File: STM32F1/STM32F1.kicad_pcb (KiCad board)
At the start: 2 copper layers, 55.9 x 22.9 mm, 40 parts, among them J1 Conn_02x03_Odd_Even, J2 Conn_01x04_Male, J3 10033526-N3212MLF, J4 Conn_01x20_Male, J5 Conn_01x20_Male, SW1 PTS 647 SK38 SMTR2 LFS, U1 RT9193, U2 STM32F103CBTx, Y1 ABL-8.000MHZ-B2‎, Y2 RSM200S-32.768-12.5-10PPM-NPB

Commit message: Boards sent to be built.
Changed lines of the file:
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@@
     (thickness 1.6)
     (drawings 58)
-    (tracks 398)
+    (tracks 393)
     (zones 0)
     (modules 40)
@@
   (segment (start 166.878 101.219) (end 166.878 101.219) (width 0.2032) (layer F.Cu) (net 3))
   (via (at 164.211 101.6) (size 0.6096) (drill 0.3048) (layers F.Cu B.Cu) (net 3))
-  (segment (start 160.909 101.727) (end 159.512 101.727) (width 0.2032) (layer B.Cu) (net 3))
-  (segment (start 164.211 101.6) (end 161.163 101.6) (width 0.2032) (layer B.Cu) (net 3))
-  (segment (start 161.036 101.727) (end 160.909 101.727) (width 0.2032) (layer B.Cu) (net 3))
-  (segment (start 161.163 101.6) (end 161.036 101.727) (width 0.2032) (layer B.Cu) (net 3))
   (segment (start 168.783 101.219) (end 164.592 101.219) (width 0.2032) (layer F.Cu) (net 3))
   (segment (start 169.771555 99.749891) (end 169.744109 99.749891) (width 0.2032) (layer F.Cu) (net 3))
@@
   (segment (start 169.744109 99.749891) (end 169.164 100.33) (width 0.2032) (layer F.Cu) (net 3))
   (segment (start 169.164 100.838) (end 168.783 101.219) (width 0.2032) (layer F.Cu) (net 3))
+  (segment (start 164.211 101.6) (end 161.163 101.6) (width 0.2032) (layer B.Cu) (net 3))
+  (segment (start 161.036 101.727) (end 159.512 101.727) (width 0.2032) (layer B.Cu) (net 3))
+  (segment (start 161.163 101.6) (end 161.036 101.727) (width 0.2032) (layer B.Cu) (net 3))
   (via (at 165.608 102.362) (size 0.9144) (drill 0.4572) (layers F.Cu B.Cu) (net 4))
   (via (at 191.389 96.8375) (size 0.6096) (drill 0.3048) (layers F.Cu B.Cu) (net 4))
@@
   (segment (start 167.64 108.712) (end 186.944 108.712) (width 0.2032) (layer B.Cu) (net 8))
   (segment (start 186.944 108.712) (end 187.96 107.696) (width 0.2032) (layer B.Cu) (net 8))
+  (segment (start 189.879 103.491) (end 189.23 104.14) (width 0.2032) (layer B.Cu) (net 9))
+  (segment (start 191.389 103.491) (end 189.879 103.491) (width 0.2032) (layer B.Cu) (net 9))
+  (segment (start 190.627 105.537) (end 189.23 104.14) (width 0.2032) (layer F.Cu) (net 9))
+  (segment (start 165.227 111.76) (end 183.896 111.76) (width 0.2032) (layer F.Cu) (net 9))
+  (segment (start 165.299105 107.050769) (end 164.476074 107.8738) (width 0.2032) (layer F.Cu) (net 9))
+  (segment (start 164.465 110.998) (end 165.227 111.76) (width 0.2032) (layer F.Cu) (net 9))
+  (segment (start 183.896 111.76) (end 184.785 110.871) (width 0.2032) (layer F.Cu) (net 9))
+  (segment (start 164.476074 107.8738) (end 164.465 107.8738) (width 0.2032) (layer F.Cu) (net 9))
+  (segment (start 184.785 110.871) (end 184.785 109.982) (width 0.2032) (layer F.Cu) (net 9))
   (segment (start 190.627 108.077) (end 190.627 105.537) (width 0.2032) (layer F.Cu) (net 9))
   (segment (start 164.465 107.8738) (end 164.465 110.998) (width 0.2032) (layer F.Cu) (net 9))
+  (segment (start 184.785 109.982) (end 185.547 109.22) (width 0.2032) (layer F.Cu) (net 9))
+  (segment (start 185.547 109.22) (end 189.484 109.22) (width 0.2032) (layer F.Cu) (net 9))
   (segment (start 189.484 109.22) (end 190.627 108.077) (width 0.2032) (layer F.Cu) (net 9))
-  (segment (start 165.227 111.76) (end 183.769 111.633) (width 0.2032) (layer F.Cu) (net 9))
-  (segment (start 165.299105 107.050769) (end 164.476074 107.8738) (width 0.2032) (layer F.Cu) (net 9))
-  (segment (start 164.465 110.998) (end 165.227 111.76) (width 0.2032) (layer F.Cu) (net 9))
-  (segment (start 183.769 111.633) (end 184.023 111.633) (width 0.2032) (layer F.Cu) (net 9))
-  (segment (start 185.547 109.22) (end 189.484 109.22) (width 0.2032) (layer F.Cu) (net 9))
-  (segment (start 164.476074 107.8738) (end 164.465 107.8738) (width 0.2032) (layer F.Cu) (net 9))
-  (segment (start 190.627 105.537) (end 189.23 104.14) (width 0.2032) (layer F.Cu) (net 9))
-  (segment (start 184.785 109.982) (end 185.547 109.22) (width 0.2032) (layer F.Cu) (net 9))
-  (segment (start 184.023 111.633) (end 184.785 110.871) (width 0.2032) (layer F.Cu) (net 9))
-  (segment (start 184.785 110.871) (end 184.785 109.982) (width 0.2032) (layer F.Cu) (net 9))
-  (segment (start 189.879 103.491) (end 189.23 104.14) (width 0.2032) (layer B.Cu) (net 9))
-  (segment (start 191.389 103.491) (end 189.879 103.491) (width 0.2032) (layer B.Cu) (net 9))
   (via (at 145.529 102.87) (size 0.6096) (drill 0.3048) (layers F.Cu B.Cu) (net 10))
   (segment (start 145.529 103.391) (end 145.529 102.87) (width 0.2032) (layer B.Cu) (net 10))
@@
   (segment (start 160.655 110.49) (end 160.655 110.28066) (width 0.2032) (layer F.Cu) (net 34))
   (segment (start 147.447 111.633) (end 146.685 110.871) (width 0.2032) (layer B.Cu) (net 34))
+  (segment (start 145.7325 108.9025) (end 145.7325 107.555) (width 0.2032) (layer B.Cu) (net 34))
+  (segment (start 146.685 109.855) (end 145.7325 108.9025) (width 0.2032) (layer B.Cu) (net 34))
+  (segment (start 146.685 110.871) (end 146.685 109.855) (width 0.2032) (layer B.Cu) (net 34))
+  (segment (start 160.655 110.617) (end 159.639 111.633) (width 0.2032) (layer B.Cu) (net 34))
+  (segment (start 160.655 110.49) (end 160.655 110.617) (width 0.2032) (layer B.Cu) (net 34))
   (segment (start 159.639 111.633) (end 147.447 111.633) (width 0.2032) (layer B.Cu) (net 34))
-  (segment (start 160.655 110.49) (end 160.655 110.617) (width 0.2032) (layer B.Cu) (net 34))
-  (segment (start 160.655 110.617) (end 159.639 111.633) (width 0.2032) (layer B.Cu) (net 34))
-  (segment (start 146.685 110.871) (end 146.685 109.855) (width 0.2032) (layer B.Cu) (net 34))
-  (segment (start 146.685 109.855) (end 145.7325 108.9025) (width 0.2032) (layer B.Cu) (net 34))
-  (segment (start 145.7325 108.9025) (end 145.7325 107.555) (width 0.2032) (layer B.Cu) (net 34))
   (segment (start 163.195 108.447766) (end 164.945551 106.697215) (width 0.2032) (layer F.Cu) (net 35))
   (segment (start 163.195 110.49) (end 163.195 108.447766) (width 0.2032) (layer F.Cu) (net 35))
   (segment (start 145.0975 112.0775) (end 144.145 111.125) (width 0.2032) (layer B.Cu) (net 35))
+  (segment (start 161.6075 112.0775) (end 145.0975 112.0775) (width 0.2032) (layer B.Cu) (net 35))
+  (segment (start 144.145 111.125) (end 144.145 107.555) (width 0.2032) (layer B.Cu) (net 35))
   (segment (start 163.195 110.49) (end 161.6075 112.0775) (width 0.2032) (layer B.Cu) (net 35))
-  (segment (start 144.145 111.125) (end 144.145 107.555) (width 0.2032) (layer B.Cu) (net 35))
-  (segment (start 161.6075 112.0775) (end 145.0975 112.0775) (width 0.2032) (layer B.Cu) (net 35))
   (segment (start 142.635 107.555) (end 144.145 107.555) (width 0.2032) (layer B.Cu) (net 35))
   (segment (start 140.335 109.855) (end 142.635 107.555) (width 0.2032) (layer B.Cu) (net 35))
@@
   (segment (start 167.132 99.314) (end 167.513 99.695) (width 0.381) (layer F.Cu) (net 52))
   (segment (start 168.412234 99.695) (end 169.064449 99.042785) (width 0.381) (layer F.Cu) (net 52))
-  (segment (start 186.055 110.49) (end 184.277 112.268) (width 0.508) (layer F.Cu) (net 53))
-  (segment (start 149.225 111.76) (end 149.225 109.728) (width 0.508) (layer F.Cu) (net 53))
-  (segment (start 149.86 112.395) (end 149.225 111.76) (width 0.508) (layer F.Cu) (net 53))
-  (segment (start 150.114 112.395) (end 149.86 112.395) (width 0.508) (layer F.Cu) (net 53))
-  (segment (start 160.655 112.395) (end 150.114 112.395) (width 0.508) (layer F.Cu) (net 53))
-  (segment (start 184.15 112.395) (end 160.655 112.395) (width 0.508) (layer F.Cu) (net 53))
-  (segment (start 184.277 112.268) (end 184.15 112.395) (width 0.508) (layer F.Cu) (net 53))
   (segment (start 149.225 109.728) (end 149.225 109.728) (width 0.508) (layer F.Cu) (net 53))
   (via (at 149.225 109.728) (size 0.6096) (drill 0.3048) (layers F.Cu B.Cu) (net 53))
   (segment (start 149.225 109.454) (end 147.574 107.803) (width 0.508) (layer B.Cu) (net 53))
   (segment (start 149.225 109.728) (end 149.225 109.454) (width 0.508) (layer B.Cu) (net 53))
+  (segment (start 149.86 112.395) (end 149.225 111.76) (width 0.508) (layer F.Cu) (net 53))
+  (segment (start 149.225 111.76) (end 149.225 109.728) (width 0.508) (layer F.Cu) (net 53))
+  (segment (start 186.055 110.49) (end 184.15 112.395) (width 0.508) (layer F.Cu) (net 53))
+  (segment (start 184.15 112.395) (end 149.86 112.395) (width 0.508) (layer F.Cu) (net 53))
   (zone (net 1) (net_name GND) (layer B.Cu) (hatch edge 0.508)
     (connect_pads (clearance 0.1524))

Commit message: Update values on PCB.
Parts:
- R10: value 10k -> 2.4k
- R11: value 10k -> 1k

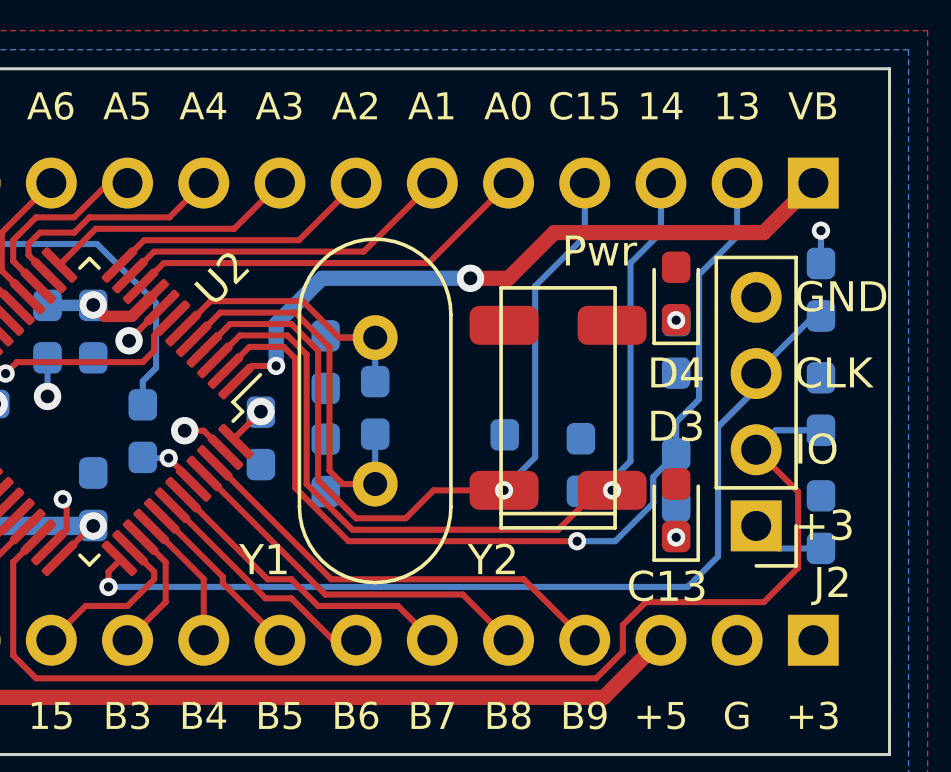
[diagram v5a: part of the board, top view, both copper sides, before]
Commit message: STM32F1 board with different crystals.
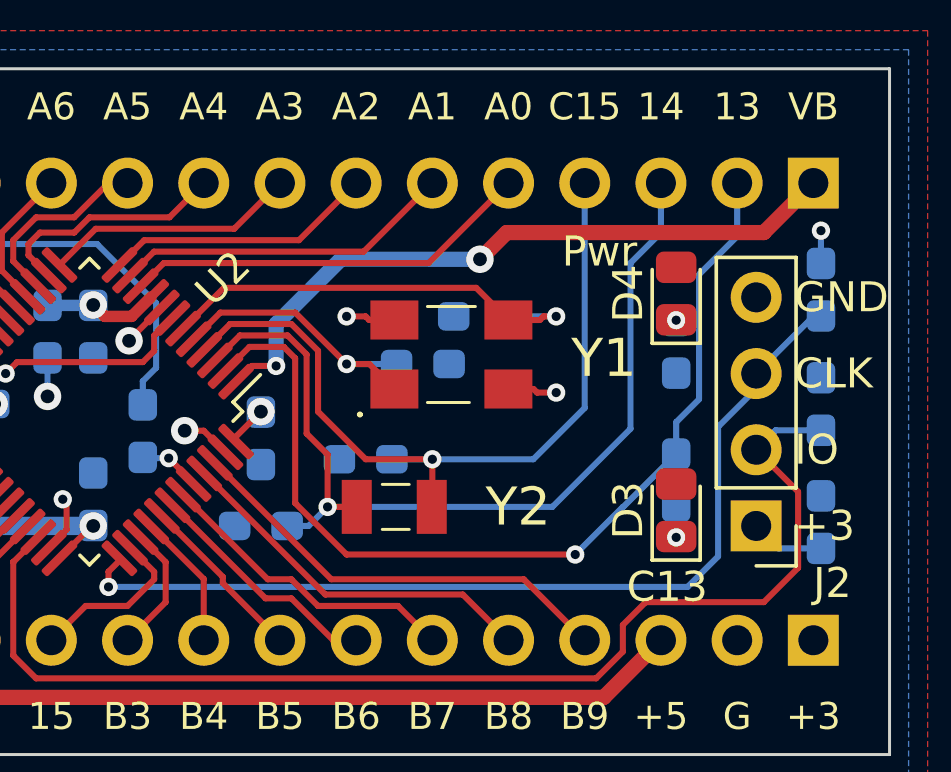
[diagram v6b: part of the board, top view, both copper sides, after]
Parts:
- removed R2: R, Resistor_SMD:R_0603_1608Metric_Pad1.05x0.95mm_HandSolder
- D3, D4: footprint LED_SMD:LED_0603_1608Metric_Pad1.05x0.95mm_HandSolder -> 0MiscParts:LED_0603_1608Metric_Pad1.05x1.35mm_HandSolder
- Y1: value ABL-8.000MHZ-B2‎ -> ABM3BAIG-8.000MHZ-1Z-T; footprint Crystal:Crystal_HC49-4H_Vertical -> SamacSys_Parts:ABM3BAIG8000MHZ1ZT
- Y2: value RSM200S-32.768-12.5-10PPM-NPB -> CM7V-T1A-32.768k-9pF-20PPM-TA-QA_T3; footprint 0MiscParts:RSM2000S -> SamacSys_Parts:CM7VT1A32768kHz125pF10PPMTBQC
- moved C3 10.9 mm to (172.7, 106.7), turned to 180 degrees
- moved Y2 6.38 mm to (177.2, 106.0), turned to 0 degrees
- moved C5 5.36 mm to (180.0, 99.7), turned to 180 degrees
- moved Y1 5.01 mm to (179.1, 101.0), turned to 0 degrees
- moved C2 4.68 mm to (178.1, 101.3), turned to 0 degrees
- moved C6 4.64 mm to (176.2, 104.5), turned to 180 degrees
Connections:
- Y1 pad 2: /D1 -> GND
- Y2 pad 2: (no net) -> /C15
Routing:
- net /D0: track 14.5 -> 9.78 mm, vias 0 -> 1
- net /D1: track 10.4 -> 15.2 mm, vias 0 -> 1
- net GND: track 28.3 -> 31.5 mm, vias 9 -> 11

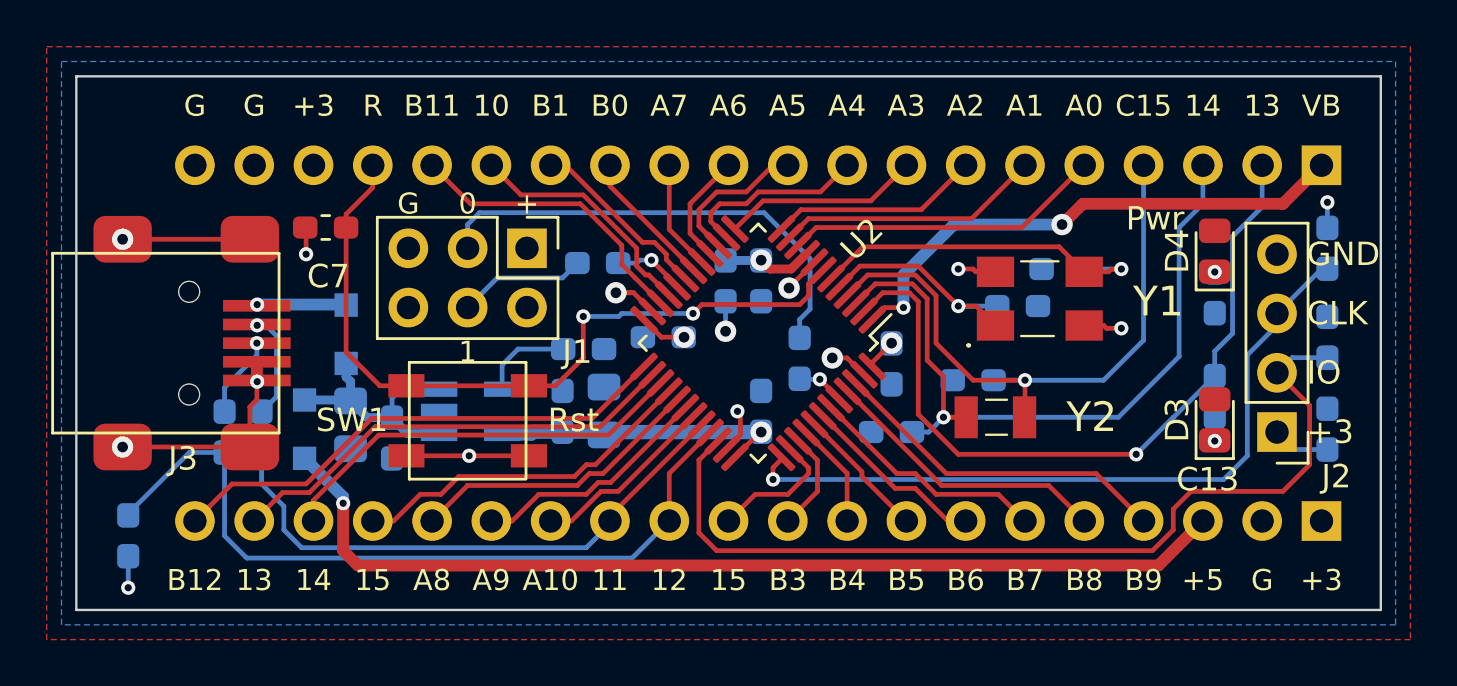
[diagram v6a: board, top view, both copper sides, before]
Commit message: STM32F1 new layout.
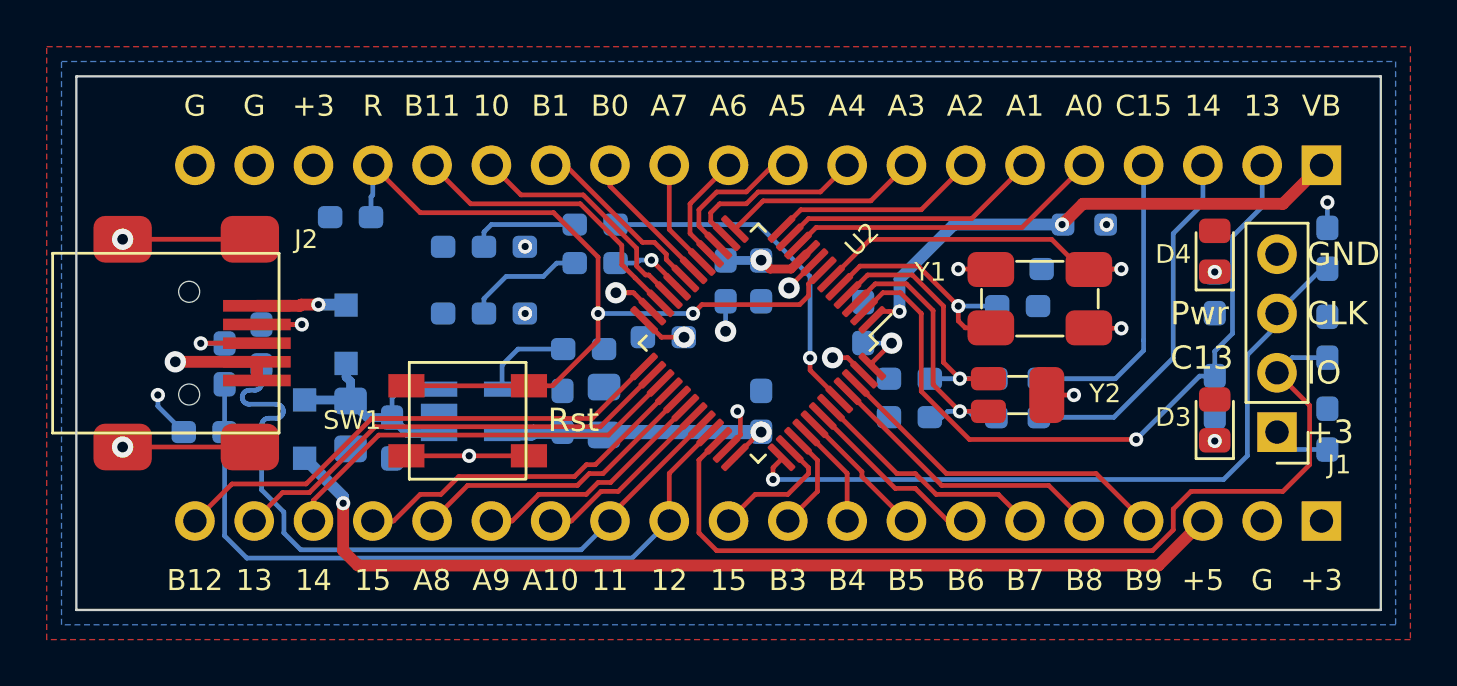
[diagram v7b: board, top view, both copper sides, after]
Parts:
- removed the J1 at (157.1, 98.8)
- removed the R9 at (140.0, 111.1)
- added JP1: Jumper_3_Open, 0MiscParts:Jumper_0603_3, B.Cu at (155.3, 98.7)
- added JP2: Jumper_3_Open, 0MiscParts:Jumper_0603_3, B.Cu at (155.3, 101.6)
- added JP3: Jumper_NO_Small, Resistor_SMD:R_0603_1608Metric_Pad0.98x0.95mm_HandSolder, B.Cu at (178.1, 106.0)
- added JP4: Jumper_NO_Small, Resistor_SMD:R_0603_1608Metric_Pad0.98x0.95mm_HandSolder, B.Cu at (178.1, 104.4)
- added JP5: Jumper_NO_Small, Resistor_SMD:R_0603_1608Metric_Pad0.98x0.95mm_HandSolder, B.Cu at (181.0, 97.8)
- added R7: 1.5k, Resistor_SMD:R_0603_1608Metric_Pad1.05x0.95mm_HandSolder, B.Cu at (143.3, 106.7)
- C5: renamed from C7; moved to B.Cu
- Y1: footprint SamacSys_Parts:ABM3BAIG8000MHZ1ZT -> 0MiscParts:Crystal_ABM3BAIG_5x3.2
- Y2: value CM7V-T1A-32.768k-9pF-20PPM-TA-QA_T3 -> Crystal_GND2_Small; footprint SamacSys_Parts:CM7VT1A32768kHz125pF10PPMTBQC -> 0MiscParts:Crystal_ECX-34G
- moved R1 10.5 mm to (160.0, 97.8), turned to 180 degrees
- moved R6 3.73 mm to (145.7, 103.0)
- moved R5 2.92 mm to (144.1, 103.8)
- moved C6 2.73 mm to (173.5, 104.4)
- moved C13 2.15 mm to (171.5, 102.0), turned to 90 degrees
- moved Y2 1.35 mm to (178.1, 105.1)
- moved C5 1.15 mm to (149.5, 97.5)
- moved C3 1.00 mm to (173.5, 106.0)
- moved R2 0.11 mm to (160.0, 99.4)
- renumbered C8 to C7, C5 to C8, J2 to J1, J3 to J2, J4 to J3, J5 to J4, R4 to R2, R5 to R3, R6 to R4, R7 to R5, R8 to R6, R10 to R8, R11 to R9
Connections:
- J3 pad 3: /C14 -> /C14Ext
- J3 pad 4: /C15 -> /C15Ext
- Y2 pad 1: /C14 -> /C15
- Y2 pad 2: /C15 -> GND
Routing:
- net /C14: track 31.4 -> 13.2 mm
- net /Boot0R: track 20.3 -> 4.65 mm
- net /C14Ext: track 0.00 -> 15.6 mm
- net /C15: track 27.2 -> 12.5 mm
- net /Boot0: track 2.08 -> 15.0 mm
- net /C15Ext: track 0.00 -> 12.9 mm
- net /A11: track 24.3 -> 31.0 mm
- net /Reset: track 32.9 -> 36.8 mm
- net /A12: track 33.5 -> 31.1 mm
- net +3V3: track 22.3 -> 24.2 mm, vias 6 -> 9
- net /C13: track 32.3 -> 30.9 mm
- net /D-: track 4.53 -> 3.69 mm
- net /D0: track 9.78 -> 10.5 mm
- net GND: track 31.5 -> 32.1 mm
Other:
- board text removed: "+"
- board text removed: "0"
- board text removed: "1"
